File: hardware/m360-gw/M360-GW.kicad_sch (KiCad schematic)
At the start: 16 parts, among them J1 Mezanino M360-RF, J2 5 V ext, J3 LEDs (painel), Q1 2N7002, SW1 Reed, U1 WEMOS D1 mini

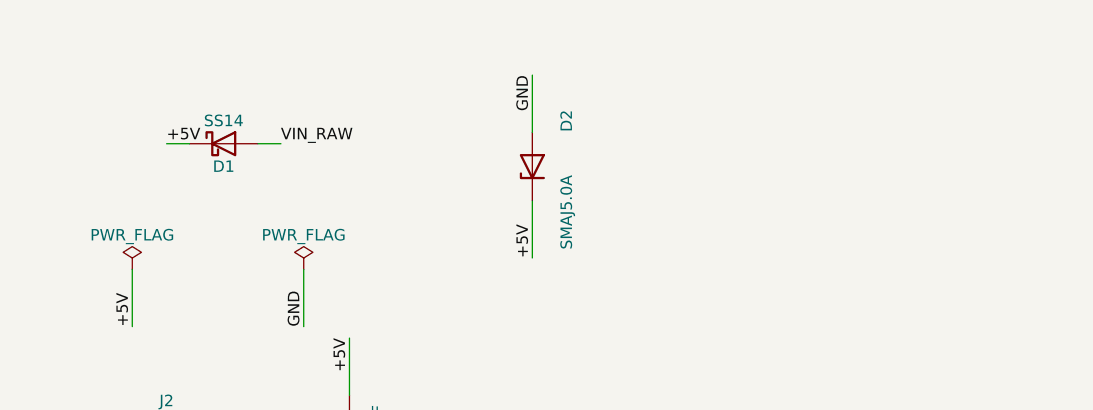
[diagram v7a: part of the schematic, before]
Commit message: fix(hardware): PTC na entrada de 5 V da ACT e da GW — correções da 4ª análise adversarial
⚠️ Só esquemáticos; as placas continuam defasadas de propósito até zerar os achados.

- ACT e GW #1: PTC F1 500 mA / 30 V (Jinrui JK-nSMD050-30, C720075) em série na entrada, depois do
  Q1 (ACT) e do SS14 (GW) e antes do TVS D2 — Q1.2 e D1.1 passam à rede VIN_POL. A ruptura mínima
  do SMAJ5.0A (6,4 V) fica acima da dos SRV05-4 (6,0 V), então sozinho o D2 não tirava os TVS de
  sinal do papel sacrificial; com o F1 a montante, a condução do D2 abre o circuito. O F1 cobre
  também o curto no chicote (a placa desarma, o quadro não cai) — §9 revista.
  Escolhido no lugar do SMD1206P050TF/15 (C106264) sugerido: mesma especificação, 427 mil em
  estoque contra 1 350, e resistência máxima de 300 mΩ contra 750 mΩ.
- ACT #2: procedimento — barramento de 5 V do quadro ajustado em 5,0 V (máx. 5,1 V), na §5.1.
- Pino 1 do RJ45: verificado por geometria e convenção pela revisão; registrada na §9 a medida de
  continuidade na primeira placa (branco-laranja T568B ↔ pad 1) antes de crimpar os chicotes.

Verificado: netdiff só com as duas redes previstas em cada placa; campos e símbolos de biblioteca
existentes inalterados (entra o Polyfuse); ERC 0; BOM com código LCSC em todas as linhas; desenho
conferido em PDF.

Co-Authored-By: Claude Opus 5 (1M context) <noreply@anthropic.com>
Claude-Session: https://claude.ai/code/session_012t7RkcrXvvpDVjKVimNu18
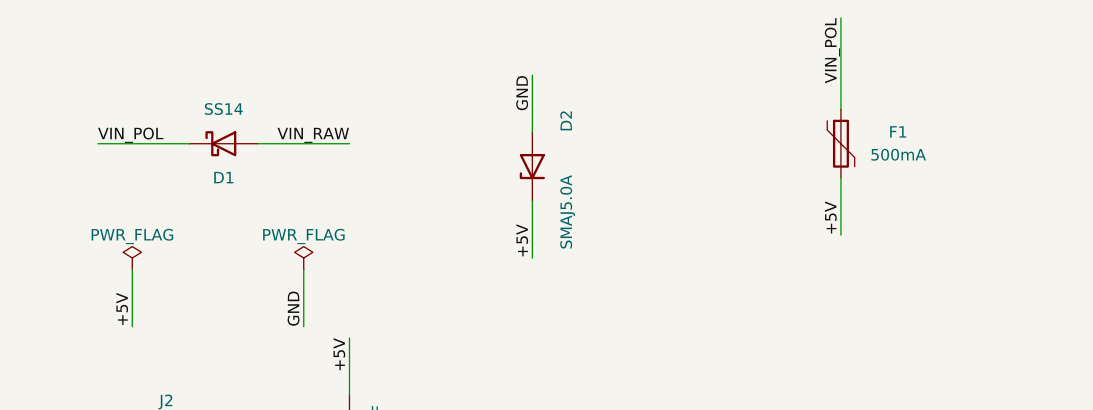
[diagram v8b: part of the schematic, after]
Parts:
- added F1: 500mA, Fuse:Fuse_1206_3216Metric, symbol Device:Polyfuse
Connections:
- net +5V: now also F1.2; no longer D1.1 (K)
- new net VIN_POL: D1.1 (K), F1.1
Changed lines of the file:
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@@
+	(wire
+		(pts
+			(xy 49.53 38.1) (xy 59.69 38.1)
+		)
+		(stroke
+			(width 0)
+			(type default)
+		)
+	)
 	(wire
 		(pts
@@
 	(wire
 		(pts
-			(xy 49.53 38.1) (xy 52.07 38.1)
+			(xy 114.3 34.29) (xy 114.3 24.13)
+		)
+		(stroke
+			(width 0)
+			(type default)
+		)
+	)
+	(wire
+		(pts
+			(xy 41.91 38.1) (xy 31.75 38.1)
+		)
+		(stroke
+			(width 0)
+			(type default)
+		)
+	)
+	(wire
+		(pts
+			(xy 114.3 41.91) (xy 114.3 48.26)
 		)
 		(stroke
@@
 		(pts
 			(xy 80.01 36.83) (xy 80.01 30.48)
-		)
-		(stroke
-			(width 0)
-			(type default)
-		)
-	)
-	(wire
-		(pts
-			(xy 41.91 38.1) (xy 39.37 38.1)
 		)
 		(stroke
@@
 		)
 	)
+	(label "VIN_RAW"
+		(at 59.69 38.1 180)
+		(effects
+			(font
+				(size 1.27 1.27)
+			)
+			(justify right bottom)
+		)
+	)
 	(label "A0_BTN"
 		(at 157.48 135.89 270)
@@
 		)
 	)
-	(label "VIN_RAW"
-		(at 52.07 38.1 0)
-		(effects
-			(font
-				(size 1.27 1.27)
-			)
-			(justify left bottom)
-		)
-	)
 	(label "NSS"
 		(at 163.83 113.03 0)
@@
 		)
 	)
-	(label "+5V"
-		(at 39.37 38.1 0)
-		(effects
-			(font
-				(size 1.27 1.27)
-			)
-			(justify left bottom)
-		)
-	)
 	(label "LED_GREEN_A"
 		(at 76.2 180.34 0)
@@
 		)
 	)
+	(label "VIN_POL"
+		(at 114.3 24.13 270)
+		(effects
+			(font
+				(size 1.27 1.27)
+			)
+			(justify right bottom)
+		)
+	)
 	(label "GND"
 		(at 189.23 115.57 180)
@@
 		)
 	)
+	(label "+5V"
+		(at 114.3 48.26 90)
+		(effects
+			(font
+				(size 1.27 1.27)
+			)
+			(justify left bottom)
+		)
+	)
 	(label "MISO"
 		(at 162.56 105.41 0)
@@
 	(label "GND"
 		(at 90.17 101.6 90)
+		(effects
+			(font
+				(size 1.27 1.27)
+			)
+			(justify left bottom)
+		)
+	)
+	(label "VIN_POL"
+		(at 31.75 38.1 0)
 		(effects
 			(font
@@
 		(dnp no)
 		(property "Reference" "D1"
-			(at 45.72 40.64 0)
+			(at 45.72 41.91 0)
 			(show_name no)
 			(do_not_autoplace no)
@@
 		)
 		(property "Value" "SS14"
-			(at 45.72 35.56 0)
+			(at 45.72 34.29 0)
 			(show_name no)
 			(do_not_autoplace no)
@@
 	)
 	(symbol
+		(lib_id "Device:Polyfuse")
+		(at 114.3 38.1 0)
+		(unit 1)
+		(body_style 1)
+		(exclude_from_sim no)
+		(in_bom yes)
+		(on_board yes)
+		(in_pos_files yes)
+		(dnp no)
+		(property "Reference" "F1"
+			(at 120.65 36.83 0)
+			(show_name no)
+			(do_not_autoplace no)
+			(effects
+				(font
+					(size 1.27 1.27)
+				)
+			)
+		)
+		(property "Value" "500mA"
+			(at 120.65 39.37 0)
+			(show_name no)
+			(do_not_autoplace no)
+			(effects
+				(font
+					(size 1.27 1.27)
+				)
+			)
+		)
+		(property "Footprint" "Fuse:Fuse_1206_3216Metric"
+			(at 114.3 38.1 0)
+			(hide yes)
+			(show_name no)
+			(do_not_autoplace no)
+			(effects
+				(font
+					(size 1.27 1.27)
+				)
+				(justify left)
+			)
+		)
+		(property "Datasheet" ""
+			(at 114.3 38.1 0)
+			(hide yes)
+			(show_name no)
+			(do_not_autoplace no)
+			(effects
+				(font
+					(size 1.27 1.27)
+				)
+			)
+		)
+		(property "Description" "Resettable fuse, polymeric positive temperature coefficient"
+			(at 114.3 38.1 0)
+			(hide yes)
+			(show_name no)
+			(do_not_autoplace no)
+			(effects
+				(font
+					(size 1.27 1.27)
+				)
+			)
+		)
+		(property "LCSC" "C720075"
+			(at 114.3 38.1 0)
+			(hide yes)
+			(show_name no)
+			(do_not_autoplace no)
+			(effects
+				(font
+					(size 1.27 1.27)
+				)
+			)
+		)
+		(pin "1"
+		)
+		(pin "2"
+		)
+		(instances
+			(project "M360-GW"
+				(path "/48a18d9a-df80-4072-896a-d7ca09082424"
+					(reference "F1")
+					(unit 1)
+				)
+			)
+		)
+	)
+	(symbol
 		(lib_id "Connector_Generic:Conn_02x05_Odd_Even")
 		(at 175.26 110.49 0)
@@
 			)
 		)
+		(property "Datasheet" ""
+			(at 80.01 40.64 0)
+			(hide yes)
+			(show_name no)
+			(do_not_autoplace no)
+			(effects
+				(font
+					(size 1.27 1.27)
+				)
+			)
+		)
+		(property "Description" "TVS unidirecional (símbolo Zener: K no +5V)"
+			(at 80.01 40.64 0)
+			(hide yes)
+			(show_name no)
+			(do_not_autoplace no)
+			(effects
+				(font
+					(size 1.27 1.27)
+				)
+			)
+		)
 		(property "LCSC" "C2925443"
 			(at 80.01 40.64 0)
 			(hide yes)
-			(effects
-				(font
-					(size 1.27 1.27)
-				)
-			)
-		)
-		(property "Datasheet" ""
-			(at 80.01 40.64 0)
-			(hide yes)
-			(show_name no)
-			(do_not_autoplace no)
-			(effects
-				(font
-					(size 1.27 1.27)
-				)
-			)
-		)
-		(property "Description" "TVS unidirecional (símbolo Zener: K no +5V)"
-			(at 80.01 40.64 0)
-			(hide yes)
